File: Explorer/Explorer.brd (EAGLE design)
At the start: 68.6 x 55.9 mm, 42 parts, among them J4 POWER_JACK

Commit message: updated explorer board
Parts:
- removed D2: 1N4001, SparkFun-DiscreteSemi:DIODE-1N4001-KIT
- removed R2: 10k, SparkFun-Resistors:0603
- removed RESET: SKRKAEE020, D3ltav's Custom:SW2-2.6-3.9X2.9X1.5+0.4MM
- added P2: (no value), SparkFun-LED:LED-0603
- added Q1, Q10, Q11, Q12, Q13, Q14, Q2, Q3, Q4, Q5, Q6, Q7, Q8, Q9: BSS138, SparkFun-DiscreteSemi:SOT23-3
- added R15, R16, R17, R18, R19, R20, R21, R22, R23, R24, R25, R26, R27, R28, R29, R30, R31, R32: 10k, SparkFun-Resistors:0603
- added U$1: (no value), D3ltav's Custom:LABEL-3#3V6
- added U$2: (no value), D3ltav's Custom:LABEL-5V5
- added U$3: (no value), D3ltav's Custom:LABEL-A01
- added U$4: (no value), D3ltav's Custom:LABEL-A10
- added U$5: (no value), D3ltav's Custom:LABEL-A23
- added U$6: (no value), D3ltav's Custom:LABEL-A34
- added U$7: (no value), D3ltav's Custom:LABEL-A45
- D1: value (none) -> 1N4001; device SparkFun-LED:LED-0603 -> SparkFun-DiscreteSemi:DIODE-1N4001-KIT
- J2: device SparkFun-Connectors:1X19 -> SparkFun-Connectors:1X20
- R1: value 1k -> 10k
- moved D1 56.1 mm to (17.8, 15.2), turned to 0 degrees
- moved R13 8.52 mm to (10.2, 33.0)
- moved R4 7.62 mm to (48.3, 36.8)
- moved R11 6.35 mm to (17.8, 33.0)
- moved R3 6.35 mm to (48.3, 33.0)
- moved R14 5.08 mm to (10.2, 36.8)
- moved R6 5.08 mm to (40.6, 36.8)
- moved R9 4.58 mm to (25.4, 33.0)
- moved R5 4.58 mm to (40.6, 33.0)
- moved R7 3.81 mm to (33.0, 33.0)
- moved SPI 3.17 mm to (6.99, 50.8)
- moved R8 2.54 mm to (33.0, 36.8)
- moved R12 2.54 mm to (17.8, 36.8)
- moved J1 1.27 mm to (63.5, 14.0)
- moved WIFI-RESET 1.27 mm to (36.8, 9.53)
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- renumbered D10 to P10, D11 to P11, D12 to P12, D13 to P13, D3 to P3, D4 to P4, D5 to P5, D6 to P6, D7 to P7, D8 to P8, D9 to P9, J4 to J8, U1 to VR1
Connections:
- removed net N$8: R2.2, RESET.2
- new net L10: Q9.3, R23.2
- new net L11: Q10.3, R24.2
- new net L12: Q11.3, R25.2
- new net L13: Q12.3, R26.2
- new net L2: Q1.3, R15.2
- new net L3: Q2.3, R16.2
- new net L4: Q3.3, R17.2
- new net L5: Q4.3, R18.2
- new net L6: Q5.3, R19.2
- new net L7: Q6.3, R20.2
- new net L8: Q7.3, R21.2
- new net L9: Q8.3, R22.2
- new net MISO: B1.MISO, SPI.3
- new net MOSI: B1.MOSI, SPI.4
- new net N$10: P13.C, R26.1
- new net N$11: P12.C, R25.1
- new net N$12: P11.C, R24.1
- new net N$13: P10.C, R23.1
- new net N$14: P9.C, R22.1
- new net N$15: P8.C, R21.1
- new net N$16: P7.C, R20.1
- new net N$17: P6.C, R19.1
- new net N$18: P5.C, R18.1
- new net N$19: P4.C, R17.1
- new net N$20: P3.C, R16.1
- new net N$21: P2.C, R15.1
- new net SCK: B1.SCK, SPI.2
- new net SCL_3V: J1.4, Q13.2, R27.1
- new net SDA_3V: J1.3, Q14.2, R28.1
- net 3.3V: now also Q13.1, Q14.1, R27.2, R28.2
- net D10: now also Q9.1
- net D11: now also Q10.1
- net D12: now also Q11.1
- net D13: now also Q12.1
- net D2: now also Q1.1
- net D20_SDA: now also Q14.3, R30.1
- net D21_SCL: now also Q13.3, R29.1
- net D3: now also Q2.1
- net D4: now also Q3.1
- net D5: now also Q4.1
- net D6: now also Q5.1
- net D7: now also Q6.1
- net D8: now also Q7.1
- net D9: now also Q8.1
- net GND: now also Q1.2, Q10.2, Q11.2, Q12.2, Q2.2, Q3.2, Q4.2, Q5.2, Q6.2, Q7.2, Q8.2, Q9.2, R31.1, R32.1; no longer R2.1
- net MEGARST: now also B1.RESET@2; no longer RESET.1
- net N$2: now also D1.A; no longer D2.A
- net N$4: now also R31.2, WIFI-RESET.2; no longer J1.3
- net N$9: now also R32.2, WIFI-BOOT.2; no longer J1.4
- net VCC: now also B1.VCC, P10.A, P11.A, P12.A, P13.A, P2.A, P3.A, P4.A, P5.A, P6.A, P7.A, P8.A, P9.A, R29.2, R30.2; no longer SPI.2
- net VIN: now also B1.VIN, D1.C; no longer D2.C
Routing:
- net VCC: track 0.00 -> 183.3 mm
- net D21_SCL: track 0.00 -> 102.8 mm, vias 0 -> 1
- net MEGARST: track 0.00 -> 100.7 mm, vias 0 -> 1
- net D20_SDA: track 0.00 -> 97.3 mm, vias 0 -> 1
- net 3.3V: track 0.00 -> 91.5 mm, vias 0 -> 1
- net MOSI: track 0.00 -> 88.7 mm
- net MISO: track 0.00 -> 86.3 mm, vias 0 -> 1
- net SCK: track 0.00 -> 81.5 mm
- net A0: track 0.00 -> 76.7 mm
- net A1: track 0.00 -> 74.4 mm
- net A2: track 0.00 -> 71.5 mm
- net A5: track 0.00 -> 70.1 mm
- net A3: track 0.00 -> 65.6 mm
- net N$15: track 0.00 -> 65.6 mm
- net A4: track 0.00 -> 62.1 mm
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- added copper zone on layer 1, net N$1
- added copper zone on layer 1, net VIN
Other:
- board text added: "ANALOG"
- board text added: "J4"
- board text added: "J5"
- board text added: "J6"
- board text added: "J7"
- board text added: "OFF"
- board text added: "ON"
- board text removed: "SSTuino II Explorer Board"

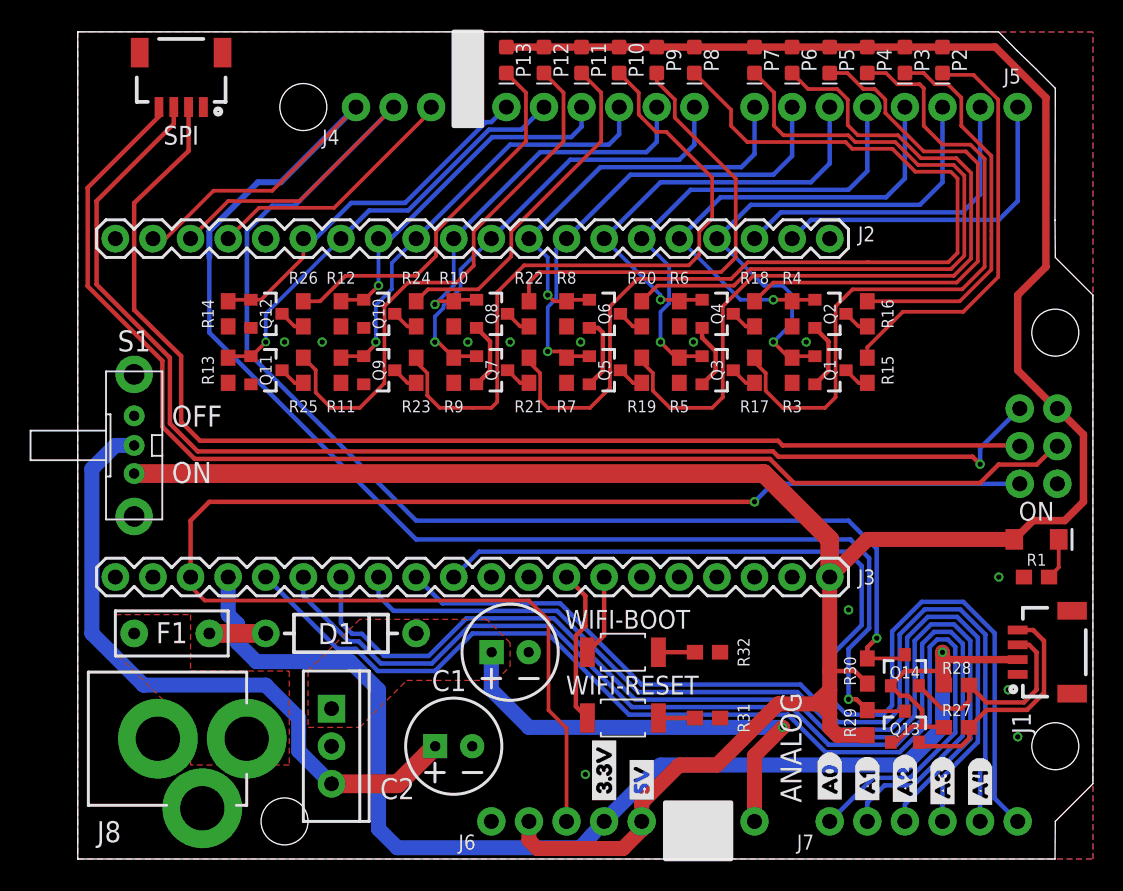
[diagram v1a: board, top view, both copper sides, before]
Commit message: updated Explorer board to first prototype version
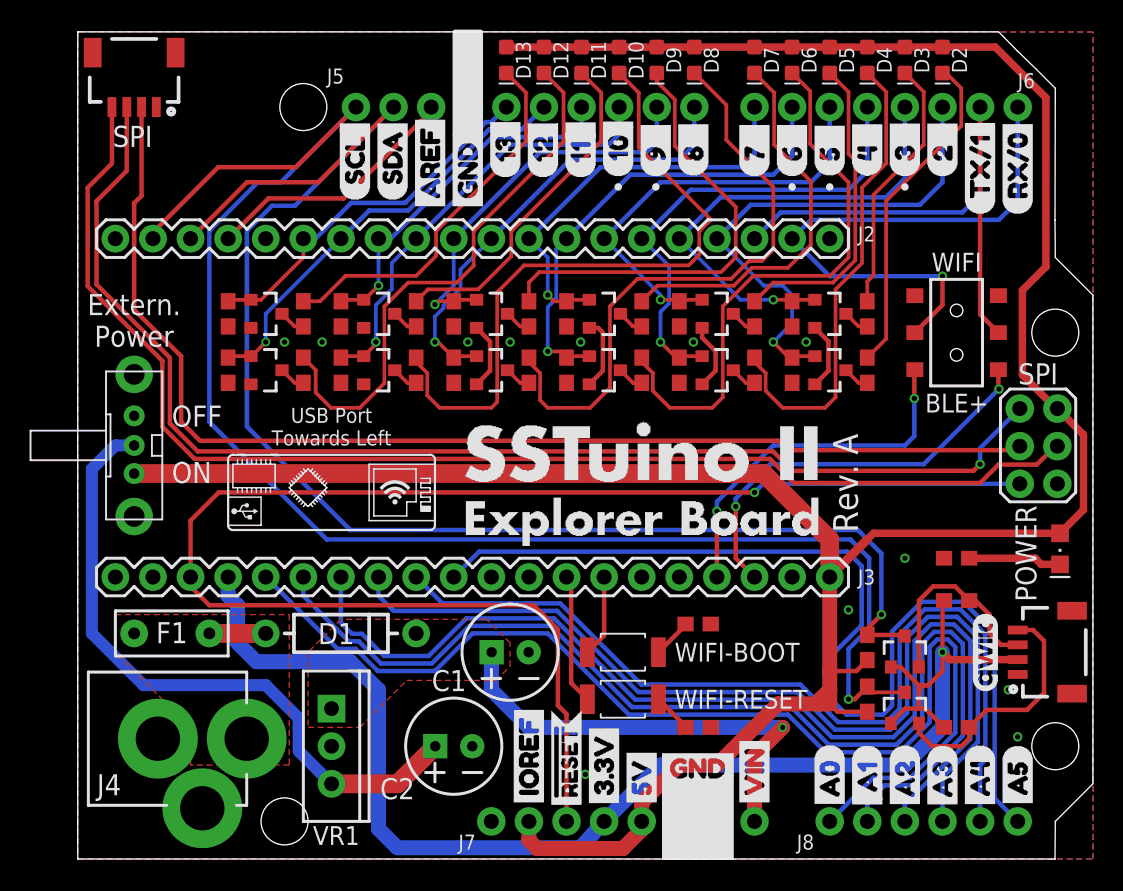
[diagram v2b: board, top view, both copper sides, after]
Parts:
- removed ON: (no value), SparkFun-LED:LED-1206
- removed R32: 10k, SparkFun-Resistors:0603
- removed SPI: (no value), SparkFun-Connectors:1X04_1MM_RA
- added D14: (no value), adafruit:CHIPLED_0805
- added J9: (no value), SparkFun-Connectors:1X04_1MM_RA
- added R2: 10k, SparkFun-Resistors:0603
- added S2: (no value), SparkFun-Switches:SWITCH_DPDT_SMD_AYZ0202
- added U$10: (no value), D3ltav's Custom:STARFIELD_URSAMINOR
- added U$11: (no value), D3ltav's Custom:STARFIELD_SMALL
- added U$12: (no value), D3ltav's Custom:STARFIELD_ORION
- added U$13: (no value), D3ltav's Custom:STARFIELD_LYRA
- added U$14: (no value), D3ltav's Custom:STARFIELD_CASSIOPEIA
- added U$15, U$16, U$17, U$18, U$19: (no value), D3ltav's Custom:STARFIELD_SMALL2
- added U$20: (no value), SSTuino II Logos:A22
- added U$21, U$45: (no value), D3ltav's Custom:EXPLORER_BOARD_LARGE
- added U$22: (no value), SSTuino II Logos:A33
- added U$23: (no value), SSTuino II Logos:A44
- added U$24: (no value), SSTuino II Logos:A55
- added U$25: (no value), SSTuino II Logos:GND6
- added U$26: (no value), SSTuino II Logos:1314
- added U$27: (no value), SSTuino II Logos:1215
- added U$28: (no value), SSTuino II Logos:1116
- added U$29: (no value), SSTuino II Logos:1017
- added U$30: (no value), SSTuino II Logos:9__18
- added U$31: (no value), SSTuino II Logos:8__19
- added U$32: (no value), SSTuino II Logos:7__20
- added U$33: (no value), SSTuino II Logos:6__21
- added U$34: (no value), SSTuino II Logos:5__22
- added U$35: (no value), SSTuino II Logos:4__23
- added U$36: (no value), SSTuino II Logos:3__24
- added U$37: (no value), SSTuino II Logos:2__25
- added U$38: (no value), SSTuino II Logos:TX#127
- added U$39: (no value), SSTuino II Logos:RX#026
- added U$40: (no value), SSTuino II Logos:AREF13
- added U$41: (no value), SSTuino II Logos:SDA25
- added U$42: (no value), SSTuino II Logos:SCL26
- added U$43: (no value), SSTuino II Logos:VIN10
- added U$44: (no value), D3ltav's Custom:QWIIC_LOGO
- added U$46: (no value), D3ltav's Custom:USBLOGO#PNG
- added U$47: (no value), D3ltav's Custom:WIFILOGO#JPG
- added U$8: (no value), D3ltav's Custom:SST-BIG
- added U$9: (no value), D3ltav's Custom:EXPLORER
- R1, R15, R16, R17, R18, R19, R20, R21, R22, R23, R24, R25, R26: value 10k -> 1k
- U$1: device D3ltav's Custom:LABEL-3#3V6 -> SSTuino II Logos:IOREF9
- U$2: device D3ltav's Custom:LABEL-5V5 -> SSTuino II Logos:3#3V7
- U$3: device D3ltav's Custom:LABEL-A01 -> SSTuino II Logos:#RESET28
- U$4: device D3ltav's Custom:LABEL-A10 -> SSTuino II Logos:5V8
- U$5: device D3ltav's Custom:LABEL-A23 -> SSTuino II Logos:GND6
- U$6: device D3ltav's Custom:LABEL-A34 -> SSTuino II Logos:A00
- U$7: device D3ltav's Custom:LABEL-A45 -> SSTuino II Logos:A11
- moved U$3 17.8 mm to (33.0, 2.86)
- moved U$5 17.3 mm to (38.9, 6.12), turned to 0 degrees
- moved U$4 15.2 mm to (38.1, 3.17)
- moved U$7 7.62 mm to (53.3, 3.40)
- moved U$6 7.62 mm to (50.8, 3.07)
- moved R28 5.71 mm to (59.4, 17.5)
- moved R1 5.54 mm to (59.4, 20.3)
- moved U$1 5.09 mm to (30.5, 3.17)
- moved U$2 2.56 mm to (35.6, 3.17)
- moved R29 1.59 mm to (53.3, 10.8)
- moved R30 1.59 mm to (53.3, 14.3)
- moved Q14 1.27 mm to (55.9, 14.0)
- moved Q13 1.27 mm to (55.9, 10.2)
- moved WIFI-RESET 1.27 mm to (36.8, 10.8)
- moved R31 0.90 mm to (41.9, 8.89)
- renumbered J8 to J4, P10 to D10, P11 to D11, P12 to D12, P13 to D13, P2 to D2, P3 to D3, P4 to D4, P5 to D5, P6 to D6, P7 to D7, P8 to D8, P9 to D9
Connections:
- net D0: now also S2.2
- net D1: now also S2.5
- net ESPRX: now also S2.4
- net ESPTX: now also S2.1
- net GND: now also J9.1, R2.1; no longer R32.1, SPI.1
- net MISO: now also J9.3; no longer SPI.3
- net MOSI: now also J9.4; no longer SPI.4
- net N$6: now also D14.C; no longer ON.C
- net N$9: now also R2.2; no longer R32.2
- net SCK: now also J9.2; no longer SPI.2
- net VCC: now also D14.A; no longer ON.A
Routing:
- net ESPRX: track 0.00 -> 28.0 mm, vias 0 -> 2
- net ESPTX: track 0.00 -> 24.8 mm, vias 0 -> 2
- net N$15: track 65.6 -> 40.9 mm
- net N$16: track 46.8 -> 26.2 mm
- net N$17: track 54.0 -> 38.1 mm
- net D0: track 22.6 -> 38.4 mm, vias 0 -> 1
- net D1: track 22.4 -> 38.1 mm
- net N$18: track 35.9 -> 21.3 mm
- net N$19: track 44.5 -> 31.9 mm
- net N$20: track 26.2 -> 17.5 mm
- net N$21: track 28.0 -> 22.5 mm
- net D21_SCL: track 102.8 -> 106.7 mm
- net N$6: track 2.81 -> 6.31 mm
- net VCC: track 183.3 -> 180.9 mm
- net ESPEN: track 10.6 -> 8.84 mm
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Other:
- board text added: "BLE+"
- board text added: "Extern. Power"
- board text added: "J8"
- board text added: "Made on Earth by Humans"
- board text added: "POWER"
- board text added: "Rev. A"
- board text added: "Revision A"
- board text added: "SPI"
- board text added: "USB Port Towards Left"
- board text added: "VR1"
- board text added: "WIFI"
- board text removed: "ANALOG"
- board text removed: "J4"

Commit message: completed modifications to Explorer board for final production
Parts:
- moved VR1 0.95 mm to (16.2, 7.62)
- moved J9 0.45 mm to (4.13, 50.5)
- moved WIFI-BOOT 0.32 mm to (36.8, 14.3)
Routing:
- net MEGARST: track 100.7 -> 112.0 mm
- net N$7: track 44.4 -> 50.9 mm
- net 3.3V: track 93.1 -> 89.4 mm
- net D0: track 38.4 -> 40.8 mm
- net A2: track 71.5 -> 70.4 mm
- net D21_SCL: track 106.7 -> 107.5 mm
- net A1: track 74.4 -> 73.6 mm
- net N$13: track 45.4 -> 44.7 mm
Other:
- board text added: "External Power"
- board text removed: "Extern. Power"

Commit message: added gerber and necessary production files
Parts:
- removed R2, R31: 10k, SparkFun-Resistors:0603
- removed WIFI-RESET: SKRKAEE020, D3ltav's Custom:SW2-2.6-3.9X2.9X1.5+0.4MM
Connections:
- removed net ESPEN: J3.13, WIFI-RESET.1
- removed net N$4: R31.2, WIFI-RESET.2
- removed net N$9: R2.2, WIFI-BOOT.2
- net GND: now also WIFI-BOOT.2; no longer R2.1, R31.1
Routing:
- net ESPEN: track 8.84 -> 0.00 mm
- net N$4: track 2.66 -> 0.00 mm
- net N$9: track 2.49 -> 0.00 mm
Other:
- board text added: "HYBR"
- board text added: "NORM"
- board text added: "Rev. A.1"
- board text removed: "BLE+"
- board text removed: "Rev. A"
- board text removed: "WIFI"
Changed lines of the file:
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@@
 <drawing>
 <settings>
-<setting alwaysvectorfont="yes"/>
+<setting alwaysvectorfont="no"/>
 <setting verticaltext="up"/>
 </settings>
@@
 <text x="17.145" y="27.94" size="1.016" layer="21" font="vector" ratio="16" align="bottom-center">USB Port
 Towards Left</text>
-<text x="52.705" y="25.4" size="1.6764" layer="21" font="vector" ratio="16" rot="R90" align="bottom-center">Rev. A</text>
+<text x="52.705" y="25.4" size="1.6764" layer="21" font="vector" ratio="16" rot="R90" align="bottom-center">Rev. A.1</text>
 <wire x1="23.8125" y1="27.305" x2="10.4775" y2="27.305" width="0.1524" layer="21"/>
 <wire x1="10.4775" y1="27.305" x2="10.16" y2="26.9875" width="0.1524" layer="21" curve="90"/>
@@
 <wire x1="15.24" y1="24.13" x2="15.08125" y2="23.97125" width="0.1016" layer="21"/>
 <wire x1="15.39875" y1="23.97125" x2="15.24" y2="23.8125" width="0.1016" layer="21"/>
-<text x="59.3725" y="39.6875" size="1.27" layer="21" font="vector" ratio="16" align="bottom-center">WIFI</text>
-<text x="59.3725" y="31.4325" size="1.27" layer="21" font="vector" ratio="16" rot="R180" align="bottom-center">BLE+</text>
+<text x="59.3725" y="39.6875" size="1.27" layer="21" font="vector" ratio="16" align="bottom-center">NORM</text>
+<text x="59.3725" y="31.4325" size="1.27" layer="21" font="vector" ratio="16" rot="R180" align="bottom-center">HYBR</text>
 <circle x="55.88" y="45.4025" radius="0.127" width="0.254" layer="21"/>
 <circle x="50.8" y="45.4025" radius="0.127" width="0.254" layer="21"/>
@@
 <attribute name="VALUE" x="17.145" y="15.494" size="0.6096" layer="27" font="vector" ratio="20" align="top-center"/>
 </element>
-<element name="WIFI-RESET" library="D3ltav's Custom" package="SW2-2.6-3.9X2.9X1.5+0.4MM" package3d_urn="urn:adsk.eagle:package:8005100/1" value="SKRKAEE020" x="36.83" y="10.795" smashed="yes">
-<attribute name="LCSC_PART" value="C455280" x="36.83" y="10.795" size="1.9304" layer="27" font="vector" ratio="14" display="off"/>
-<attribute name="MPN" value="SKRKAEE020" x="36.83" y="10.795" size="1.9304" layer="27" font="vector" ratio="14" display="off"/>
-<attribute name="NAME" x="40.3225" y="10.795" size="1.27" layer="25" font="vector" ratio="16" align="center-left"/>
-<attribute name="VALUE" x="35.33" y="8.505" size="0.635" layer="27" font="vector" ratio="11"/>
-</element>
 <element name="WIFI-BOOT" library="D3ltav's Custom" package="SW2-2.6-3.9X2.9X1.5+0.4MM" package3d_urn="urn:adsk.eagle:package:8005100/1" value="SKRKAEE020" x="36.83" y="14.2875" smashed="yes">
 <attribute name="LCSC_PART" value="C455280" x="36.83" y="14.2875" size="1.9304" layer="27" font="vector" ratio="14" display="off"/>
@@
 <attribute name="PROD_ID" value="RES-00824" x="53.34" y="14.2875" size="1.6764" layer="27" ratio="16" rot="R270" display="off"/>
 <attribute name="VALUE" x="52.578" y="14.2875" size="0.6096" layer="27" font="vector" ratio="20" rot="R270" align="top-center"/>
-</element>
-<element name="R31" library="SparkFun-Resistors" library_urn="urn:adsk.eagle:library:532" package="0603" package3d_urn="urn:adsk.eagle:package:39650/1" value="10k" x="41.91" y="8.89" smashed="yes" rot="R180">
-<attribute name="LCSC_PART" value="C25804" x="41.91" y="8.89" size="0.8128" layer="27" ratio="16" rot="R180" display="off"/>
-<attribute name="PROD_ID" value="RES-00824" x="41.91" y="8.89" size="0.8128" layer="27" ratio="16" rot="R180" display="off"/>
-<attribute name="VALUE" x="41.91" y="9.652" size="0.6096" layer="27" font="vector" ratio="20" rot="R180" align="top-center"/>
-</element>
-<element name="R2" library="SparkFun-Resistors" library_urn="urn:adsk.eagle:library:532" package="0603" package3d_urn="urn:adsk.eagle:package:39650/1" value="10k" x="41.91" y="15.875" smashed="yes" rot="R180">
-<attribute name="LCSC_PART" value="C25804" x="41.91" y="15.875" size="0.8128" layer="27" ratio="16" rot="R180" display="off"/>
-<attribute name="PROD_ID" value="RES-00824" x="41.91" y="15.875" size="0.8128" layer="27" ratio="16" rot="R180" display="off"/>
-<attribute name="VALUE" x="41.91" y="16.637" size="0.6096" layer="27" font="vector" ratio="20" rot="R180" align="top-center"/>
 </element>
 <element name="U$8" library="D3ltav's Custom" package="SST-BIG" value="" x="59.69" y="5.08" smashed="yes" rot="MR0"/>
@@
 <via x="26.3525" y="34.925" extent="1-16" drill="0.35" diameter="0.65"/>
 <via x="29.21" y="34.925" extent="1-16" drill="0.35" diameter="0.65"/>
-<contactref element="R31" pad="1"/>
-<contactref element="R2" pad="1"/>
 <via x="62.865" y="11.43" extent="1-16" drill="0.35" diameter="0.65"/>
 <via x="49.2125" y="34.925" extent="1-16" drill="0.35" diameter="0.65"/>
@@
 <via x="33.9725" y="34.925" extent="1-16" drill="0.35" diameter="0.65"/>
 <via x="13.97" y="34.925" extent="1-16" drill="0.35" diameter="0.65"/>
+<contactref element="WIFI-BOOT" pad="2"/>
 </signal>
 <signal name="VCC">
@@
 <wire x1="35.56" y1="15.4175" x2="35.56" y2="19.05" width="0.3048" layer="1"/>
 </signal>
-<signal name="ESPEN">
-<contactref element="J3" pad="13"/>
-<contactref element="WIFI-RESET" pad="1"/>
-<wire x1="33.02" y1="19.05" x2="33.3331" y2="18.7369" width="0.3048" layer="1"/>
-<wire x1="34.43" y1="10.795" x2="33.3331" y2="11.8919" width="0.3048" layer="1"/>
-<wire x1="33.3331" y1="18.7369" x2="33.3331" y2="11.8919" width="0.3048" layer="1"/>
-</signal>
 <signal name="ESPSCL">
 <contactref element="J3" pad="12"/>
@@
 <wire x1="3.81" y1="37.465" x2="3.81" y2="44.9025" width="0.3048" layer="1"/>
 </signal>
-<signal name="N$4">
-<contactref element="WIFI-RESET" pad="2"/>
-<contactref element="R31" pad="2"/>
-<wire x1="41.06" y1="8.89" x2="41.06" y2="8.965" width="0.3048" layer="1"/>
-<wire x1="41.06" y1="8.965" x2="39.23" y2="10.795" width="0.3048" layer="1"/>
-</signal>
-<signal name="N$9">
-<contactref element="WIFI-BOOT" pad="2"/>
-<contactref element="R2" pad="2"/>
-<wire x1="41.06" y1="15.875" x2="40.8175" y2="15.875" width="0.3048" layer="1"/>
-<wire x1="40.8175" y1="15.875" x2="39.23" y2="14.2875" width="0.3048" layer="1"/>
-</signal>
 </signals>
